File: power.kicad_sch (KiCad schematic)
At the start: 48 parts, among them J6 Ride Through, Q3 2N7002, U2 MAX17614, U3 TVS3300DRV, U4 LM61480

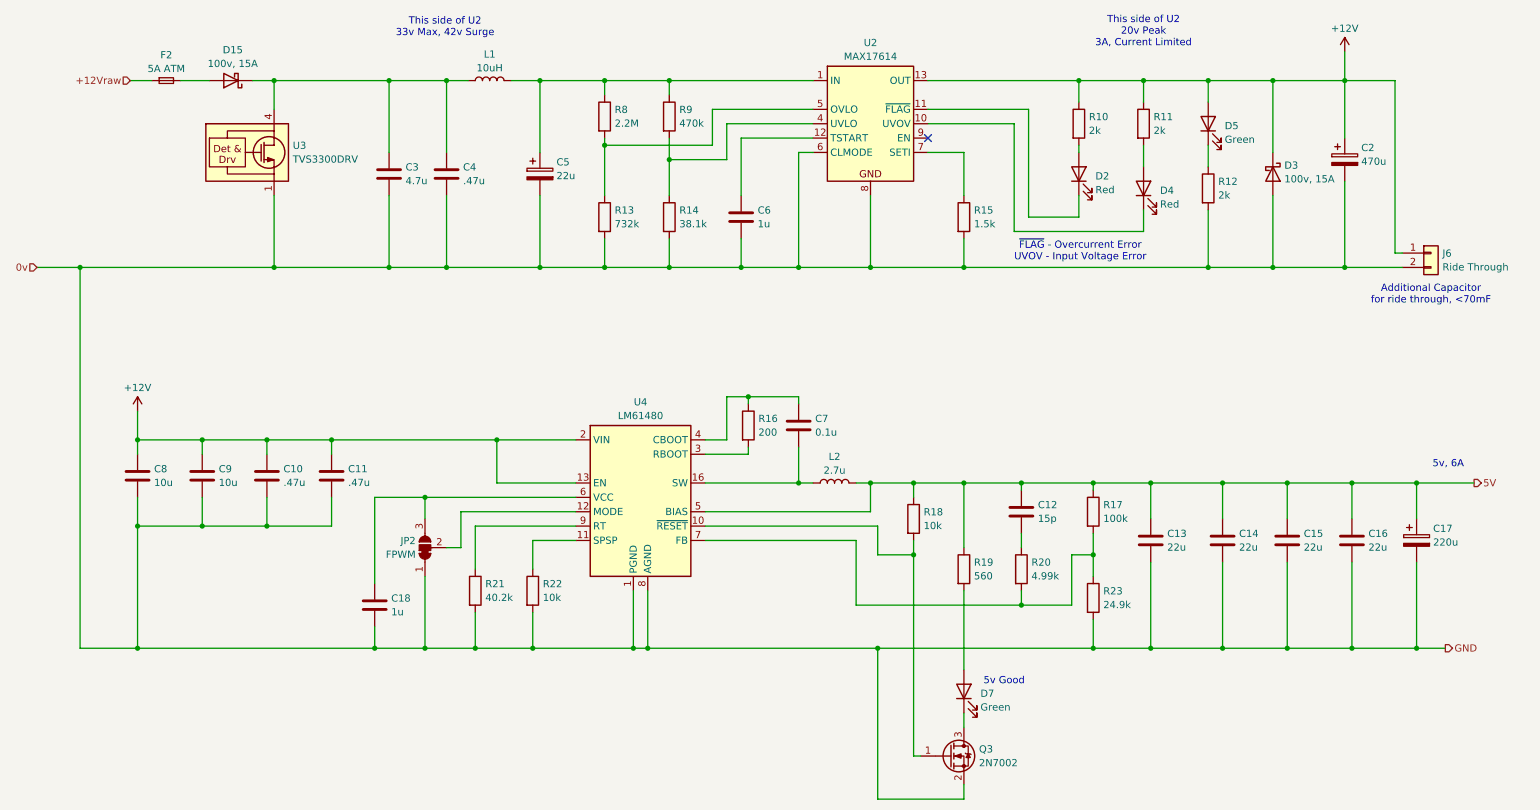
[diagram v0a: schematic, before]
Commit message: added 4 inputs and 2 pwm outputs, completed routing
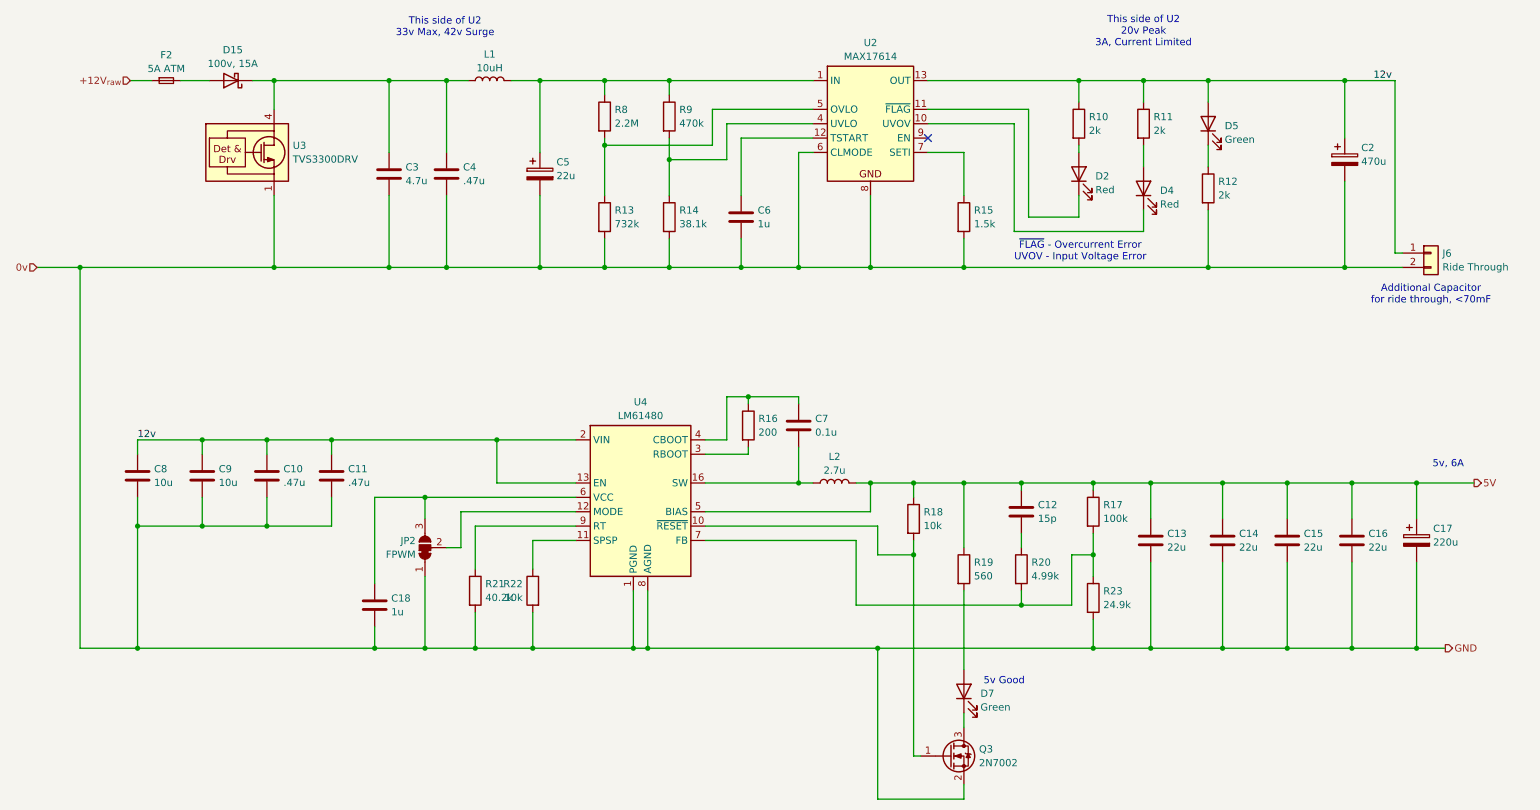
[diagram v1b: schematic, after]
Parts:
- removed D3: 100v, 15A, Package_TO_SOT_SMD:TO-277A, symbol Device:D_Schottky
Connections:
- net +12V renamed VIN
- net +12Vraw renamed +12V_{raw}

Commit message: revised schematic after initial layout  - all connectors are vertical  - increased current handling of outputs  - replaced mechanical relay with ssr  - jumper to disable gps antenna power
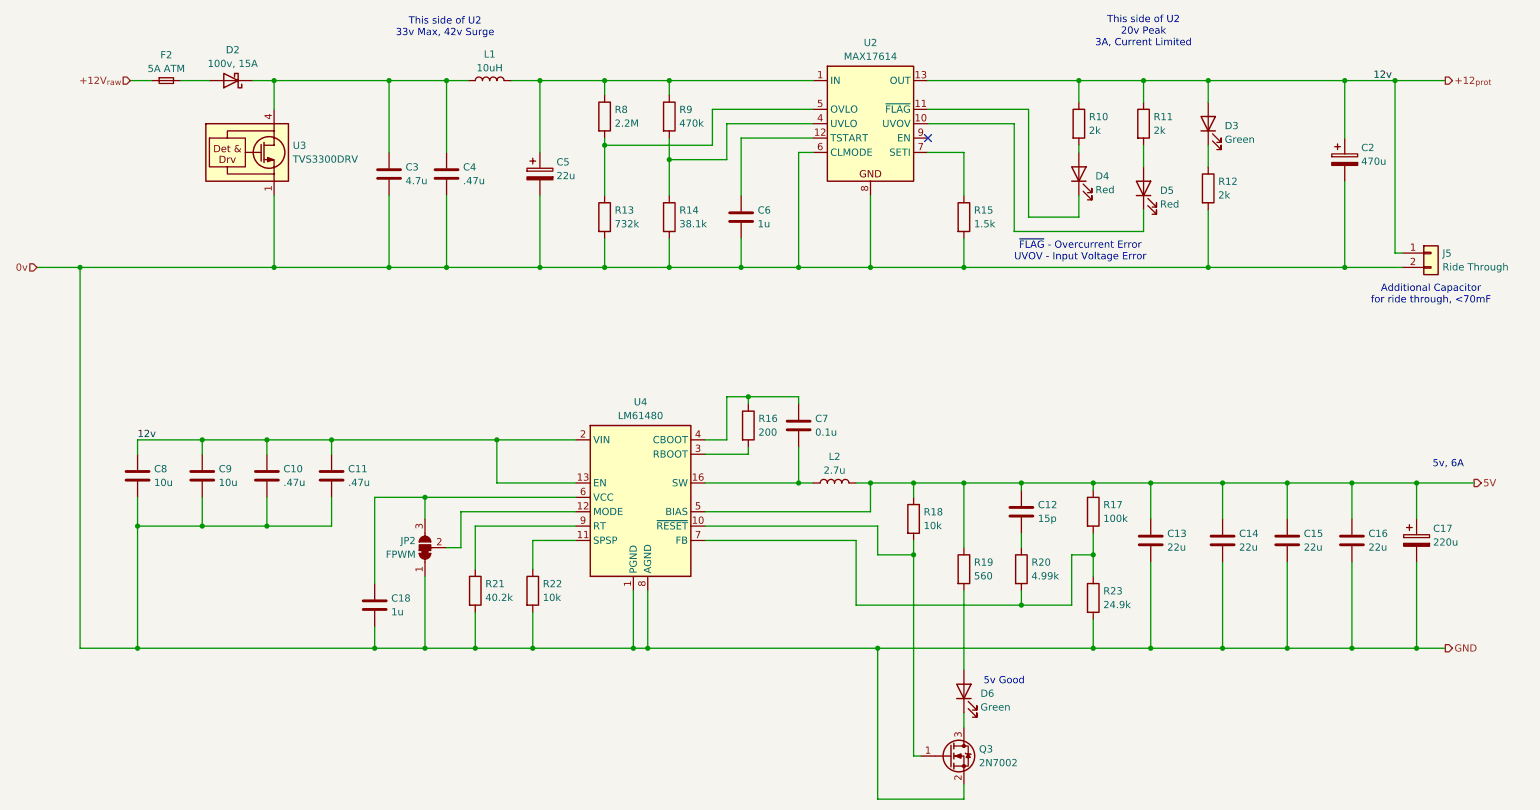
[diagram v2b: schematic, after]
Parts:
- C10, C11, C4: footprint Capacitor_SMD:C_0805_2012Metric_Pad1.18x1.45mm_HandSolder -> Capacitor_SMD:C_0805_2012Metric
- C12, C18, C6, C7: footprint Capacitor_SMD:C_0603_1608Metric_Pad1.08x0.95mm_HandSolder -> Capacitor_SMD:C_0603_1608Metric
- C13, C14, C15, C16, C8, C9: footprint Capacitor_SMD:C_1210_3225Metric_Pad1.33x2.70mm_HandSolder -> Capacitor_SMD:C_1210_3225Metric
- C3: footprint Capacitor_SMD:C_1206_3216Metric_Pad1.33x1.80mm_HandSolder -> Capacitor_SMD:C_1206_3216Metric
- D3: renamed from D5; footprint LED_SMD:LED_0603_1608Metric_Pad1.05x0.95mm_HandSolder -> LED_SMD:LED_0603_1608Metric
- D4: renamed from D2; footprint LED_SMD:LED_0603_1608Metric_Pad1.05x0.95mm_HandSolder -> LED_SMD:LED_0603_1608Metric
- D5: renamed from D4; footprint LED_SMD:LED_0603_1608Metric_Pad1.05x0.95mm_HandSolder -> LED_SMD:LED_0603_1608Metric
- D6: renamed from D7; footprint LED_SMD:LED_0603_1608Metric_Pad1.05x0.95mm_HandSolder -> LED_SMD:LED_0603_1608Metric
- R10, R11, R12, R13, R14, R15, R16, R17, R18, R19, R20, R21, R22, R23, R8, R9: footprint Resistor_SMD:R_0603_1608Metric_Pad0.98x0.95mm_HandSolder -> Resistor_SMD:R_0603_1608Metric
- renumbered D15 to D2, J6 to J5
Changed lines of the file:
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@@
 	)
 	(junction
+		(at 260.35 33.02)
+		(diameter 0)
+		(color 0 0 0 0)
+	)
+	(junction
 		(at 107.95 133.35)
 		(diameter 0)
@@
 	(wire
 		(pts
+			(xy 260.35 33.02) (xy 269.24 33.02)
+		)
+		(stroke
+			(width 0)
+			(type default)
+		)
+	)
+	(wire
+		(pts
 			(xy 168.91 160.02) (xy 168.91 133.35)
 		)
@@
 		)
 	)
+	(hierarchical_label "+12_{prot}"
+		(shape output)
+		(at 269.24 33.02 0)
+		(fields_autoplaced yes)
+		(effects
+			(font
+				(size 1.27 1.27)
+			)
+			(justify left)
+		)
+	)
 	(hierarchical_label "5V"
 		(shape output)
@@
 			)
 		)
-		(property "Footprint" "Resistor_SMD:R_0603_1608Metric_Pad0.98x0.95mm_HandSolder"
+		(property "Footprint" "Resistor_SMD:R_0603_1608Metric"
 			(at 130.302 57.15 90)
 			(effects
@@
 		(dnp no)
 		(fields_autoplaced yes)
-		(property "Reference" "D4"
+		(property "Reference" "D5"
 			(at 218.821 52.4453 90)
 			(effects
@@
 			)
 		)
-		(property "Footprint" "LED_SMD:LED_0603_1608Metric_Pad1.05x0.95mm_HandSolder"
+		(property "Footprint" "LED_SMD:LED_0603_1608Metric"
 			(at 215.9 52.07 0)
 			(effects
@@
 			(project "dashHat"
 				(path "/e63e39d7-6ac0-4ffd-8aa3-1841a4541b55/c83fc454-3a65-469f-ae3e-cbb574f94c8f"
-					(reference "D4")
+					(reference "D5")
 					(unit 1)
 				)
@@
 		(dnp no)
 		(fields_autoplaced yes)
-		(property "Reference" "J6"
+		(property "Reference" "J5"
 			(at 268.732 63.5578 0)
 			(effects
@@
 			(project "dashHat"
 				(path "/e63e39d7-6ac0-4ffd-8aa3-1841a4541b55/c83fc454-3a65-469f-ae3e-cbb574f94c8f"
-					(reference "J6")
+					(reference "J5")
 					(unit 1)
 				)
@@
 		(dnp no)
 		(fields_autoplaced yes)
-		(property "Reference" "D7"
+		(property "Reference" "D6"
 			(at 187.071 141.3453 90)
 			(effects
@@
 			)
 		)
-		(property "Footprint" "LED_SMD:LED_0603_1608Metric_Pad1.05x0.95mm_HandSolder"
+		(property "Footprint" "LED_SMD:LED_0603_1608Metric"
 			(at 184.15 140.97 0)
 			(effects
@@
 			(project "dashHat"
 				(path "/e63e39d7-6ac0-4ffd-8aa3-1841a4541b55/c83fc454-3a65-469f-ae3e-cbb574f94c8f"
-					(reference "D7")
+					(reference "D6")
 					(unit 1)
 				)
@@
 			)
 		)
-		(property "Footprint" "Resistor_SMD:R_0603_1608Metric_Pad0.98x0.95mm_HandSolder"
+		(property "Footprint" "Resistor_SMD:R_0603_1608Metric"
 			(at 173.482 110.49 90)
 			(effects
@@
 			)
 		)
-		(property "Footprint" "Resistor_SMD:R_0603_1608Metric_Pad0.98x0.95mm_HandSolder"
+		(property "Footprint" "Resistor_SMD:R_0603_1608Metric"
 			(at 214.122 40.64 90)
 			(effects
@@
 			)
 		)
-		(property "Footprint" "Capacitor_SMD:C_0603_1608Metric_Pad1.08x0.95mm_HandSolder"
+		(property "Footprint" "Capacitor_SMD:C_0603_1608Metric"
 			(at 145.7452 60.96 0)
 			(effects
@@
 			)
 		)
-		(property "Footprint" "Resistor_SMD:R_0603_1608Metric_Pad0.98x0.95mm_HandSolder"
+		(property "Footprint" "Resistor_SMD:R_0603_1608Metric"
 			(at 118.872 57.15 90)
 			(effects
@@
 			)
 		)
-		(property "Footprint" "Capacitor_SMD:C_1210_3225Metric_Pad1.33x2.70mm_HandSolder"
+		(property "Footprint" "Capacitor_SMD:C_1210_3225Metric"
 			(at 218.1352 118.11 0)
 			(effects
@@
 			)
 		)
-		(property "Footprint" "Resistor_SMD:R_0603_1608Metric_Pad0.98x0.95mm_HandSolder"
+		(property "Footprint" "Resistor_SMD:R_0603_1608Metric"
 			(at 205.232 124.46 90)
 			(effects
@@
 		(lib_id "Device:R")
 		(at 107.95 123.19 0)
-		(mirror y)
 		(unit 1)
 		(exclude_from_sim no)
@@
 		(dnp no)
 		(property "Reference" "R22"
-			(at 106.172 121.9778 0)
+			(at 109.728 121.9778 0)
 			(effects
 				(font
@@
 		)
 		(property "Value" "10k"
-			(at 106.172 124.4021 0)
+			(at 109.728 124.4021 0)
 			(effects
 				(font
@@
 			)
 		)
-		(property "Footprint" "Resistor_SMD:R_0603_1608Metric_Pad0.98x0.95mm_HandSolder"
-			(at 109.728 123.19 90)
+		(property "Footprint" "Resistor_SMD:R_0603_1608Metric"
+			(at 106.172 123.19 90)
 			(effects
 				(font
@@
 			)
 		)
-		(property "Footprint" "Resistor_SMD:R_0603_1608Metric_Pad0.98x0.95mm_HandSolder"
+		(property "Footprint" "Resistor_SMD:R_0603_1608Metric"
 			(at 118.872 39.37 90)
 			(effects
@@
 			)
 		)
-		(property "Footprint" "Capacitor_SMD:C_0603_1608Metric_Pad1.08x0.95mm_HandSolder"
+		(property "Footprint" "Capacitor_SMD:C_0603_1608Metric"
 			(at 80.9752 129.54 0)
 			(effects
@@
 			)
 		)
-		(property "Footprint" "Capacitor_SMD:C_1210_3225Metric_Pad1.33x2.70mm_HandSolder"
+		(property "Footprint" "Capacitor_SMD:C_1210_3225Metric"
 			(at 242.2652 118.11 0)
 			(effects
@@
 		(dnp no)
 		(fields_autoplaced yes)
-		(property "Reference" "D2"
+		(property "Reference" "D4"
 			(at 207.391 49.9053 90)
 			(effects
@@
 			)
 		)
-		(property "Footprint" "LED_SMD:LED_0603_1608Metric_Pad1.05x0.95mm_HandSolder"
+		(property "Footprint" "LED_SMD:LED_0603_1608Metric"
 			(at 204.47 49.53 0)
 			(effects
@@
 			(project "dashHat"
 				(path "/e63e39d7-6ac0-4ffd-8aa3-1841a4541b55/c83fc454-3a65-469f-ae3e-cbb574f94c8f"
-					(reference "D2")
+					(reference "D4")
 					(unit 1)
 				)
@@
 			)
 		)
-		(property "Footprint" "Capacitor_SMD:C_1210_3225Metric_Pad1.33x2.70mm_HandSolder"
+		(property "Footprint" "Capacitor_SMD:C_1210_3225Metric"
 			(at 50.4952 106.68 0)
 			(effects
@@
 			)
 		)
-		(property "Footprint" "Resistor_SMD:R_0603_1608Metric_Pad0.98x0.95mm_HandSolder"
+		(property "Footprint" "Resistor_SMD:R_0603_1608Metric"
 			(at 144.272 93.98 90)
 			(effects
@@
 			)
 		)
-		(property "Footprint" "Resistor_SMD:R_0603_1608Metric_Pad0.98x0.95mm_HandSolder"
+		(property "Footprint" "Resistor_SMD:R_0603_1608Metric"
 			(at 96.012 123.19 90)
 			(effects
@@
 			)
 		)
-		(property "Footprint" "Capacitor_SMD:C_1210_3225Metric_Pad1.33x2.70mm_HandSolder"
+		(property "Footprint" "Capacitor_SMD:C_1210_3225Metric"
 			(at 230.8352 118.11 0)
 			(effects
@@
 			)
 		)
-		(property "Footprint" "Resistor_SMD:R_0603_1608Metric_Pad0.98x0.95mm_HandSolder"
+		(property "Footprint" "Resistor_SMD:R_0603_1608Metric"
 			(at 192.532 119.38 90)
 			(effects
@@
 		(dnp no)
 		(fields_autoplaced yes)
-		(property "Reference" "D15"
+		(property "Reference" "D2"
 			(at 54.9275 27.6055 0)
 			(effects
@@
 			(project "dashHat"
 				(path "/e63e39d7-6ac0-4ffd-8aa3-1841a4541b55/c83fc454-3a65-469f-ae3e-cbb574f94c8f"
-					(reference "D15")
+					(reference "D2")
 					(unit 1)
 				)
@@
 			)
 		)
-		(property "Footprint" "Capacitor_SMD:C_1210_3225Metric_Pad1.33x2.70mm_HandSolder"
+		(property "Footprint" "Capacitor_SMD:C_1210_3225Metric"
 			(at 253.6952 118.11 0)
 			(effects
@@
 			)
 		)
-		(property "Footprint" "Capacitor_SMD:C_0603_1608Metric_Pad1.08x0.95mm_HandSolder"
+		(property "Footprint" "Capacitor_SMD:C_0603_1608Metric"
 			(at 193.3448 105.41 0)
 			(effects
@@
 			)
 		)
-		(property "Footprint" "Resistor_SMD:R_0603_1608Metric_Pad0.98x0.95mm_HandSolder"
+		(property "Footprint" "Resistor_SMD:R_0603_1608Metric"
 			(at 205.232 109.22 90)
 			(effects
@@
 			)
 		)
-		(property "Footprint" "Resistor_SMD:R_0603_1608Metric_Pad0.98x0.95mm_HandSolder"
+		(property "Footprint" "Resistor_SMD:R_0603_1608Metric"
 			(at 130.302 39.37 90)
 			(effects
@@
 			)
 		)
-		(property "Footprint" "Capacitor_SMD:C_0805_2012Metric_Pad1.18x1.45mm_HandSolder"
+		(property "Footprint" "Capacitor_SMD:C_0805_2012Metric"
 			(at 93.6752 53.34 0)
 			(effects
@@
 			)
 		)
-		(property "Footprint" "Resistor_SMD:R_0603_1608Metric_Pad0.98x0.95mm_HandSolder"
+		(property "Footprint" "Resistor_SMD:R_0603_1608Metric"
 			(at 202.692 40.64 90)
 			(effects
@@
 			)
 		)
-		(property "Footprint" "Capacitor_SMD:C_1206_3216Metric_Pad1.33x1.80mm_HandSolder"
+		(property "Footprint" "Capacitor_SMD:C_1206_3216Metric"
 			(at 83.5152 53.34 0)
 			(effects
@@
 			)
 		)
-		(property "Footprint" "Capacitor_SMD:C_0805_2012Metric_Pad1.18x1.45mm_HandSolder"
+		(property "Footprint" "Capacitor_SMD:C_0805_2012Metric"
 			(at 73.3552 106.68 0)
 			(effects
@@
 		(dnp no)
 		(fields_autoplaced yes)
-		(property "Reference" "D5"
+		(property "Reference" "D3"
 			(at 230.251 41.0153 90)
 			(effects
@@
 			)
 		)
-		(property "Footprint" "LED_SMD:LED_0603_1608Metric_Pad1.05x0.95mm_HandSolder"
+		(property "Footprint" "LED_SMD:LED_0603_1608Metric"
 			(at 227.33 40.64 0)
 			(effects
@@
 			(project "dashHat"
 				(path "/e63e39d7-6ac0-4ffd-8aa3-1841a4541b55/c83fc454-3a65-469f-ae3e-cbb574f94c8f"
-					(reference "D5")
+					(reference "D3")
 					(unit 1)
 				)
@@
 			)
 		)
-		(property "Footprint" "Resistor_SMD:R_0603_1608Metric_Pad0.98x0.95mm_HandSolder"
+		(property "Footprint" "Resistor_SMD:R_0603_1608Metric"
 			(at 225.552 52.07 90)
 			(effects
@@
 			)
 		)
-		(property "Footprint" "Capacitor_SMD:C_0805_2012Metric_Pad1.18x1.45mm_HandSolder"
+		(property "Footprint" "Capacitor_SMD:C_0805_2012Metric"
 			(at 61.9252 106.68 0)
 			(effects
@@
 			)
 		)
-		(property "Footprint" "Capacitor_SMD:C_1210_3225Metric_Pad1.33x2.70mm_HandSolder"
+		(property "Footprint" "Capacitor_SMD:C_1210_3225Metric"
 			(at 39.0652 106.68 0)
 			(effects
@@
 			)
 		)
-		(property "Footprint" "Capacitor_SMD:C_0603_1608Metric_Pad1.08x0.95mm_HandSolder"
+		(property "Footprint" "Capacitor_SMD:C_0603_1608Metric"
 			(at 155.9052 97.79 0)
 			(effects
@@
 			)
 		)
-		(property "Footprint" "Resistor_SMD:R_0603_1608Metric_Pad0.98x0.95mm_HandSolder"
+		(property "Footprint" "Resistor_SMD:R_0603_1608Metric"
 			(at 182.372 57.15 90)
 			(effects
@@
 			)
 		)
-		(property "Footprint" "Resistor_SMD:R_0603_1608Metric_Pad0.98x0.95mm_HandSolder"
+		(property "Footprint" "Resistor_SMD:R_0603_1608Metric"
 			(at 182.372 119.38 90)
 			(effects
